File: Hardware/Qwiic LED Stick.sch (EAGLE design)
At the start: 38 parts, among them J2 QWIIC_RA, J4 QWIIC_RA, J6 AVR_SPI_PROG_3X2TESTPOINTS, U2 ATTINY85

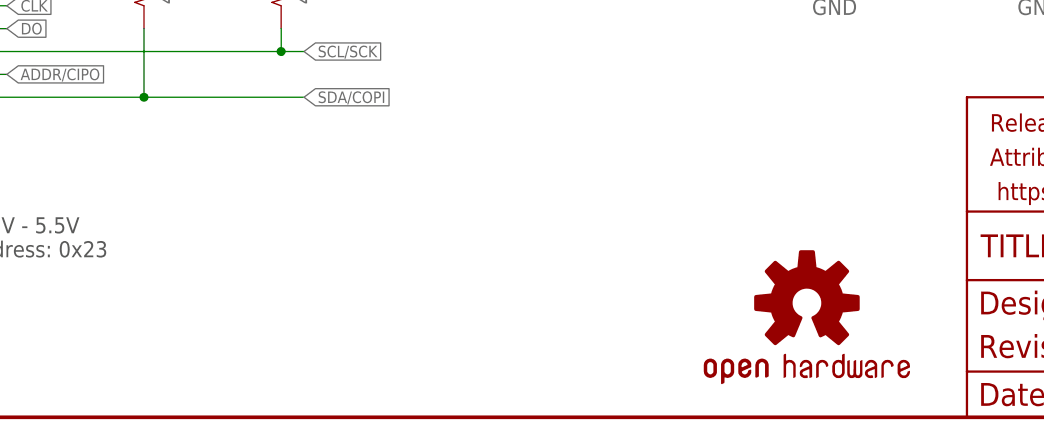
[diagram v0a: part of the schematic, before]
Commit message: Update logos
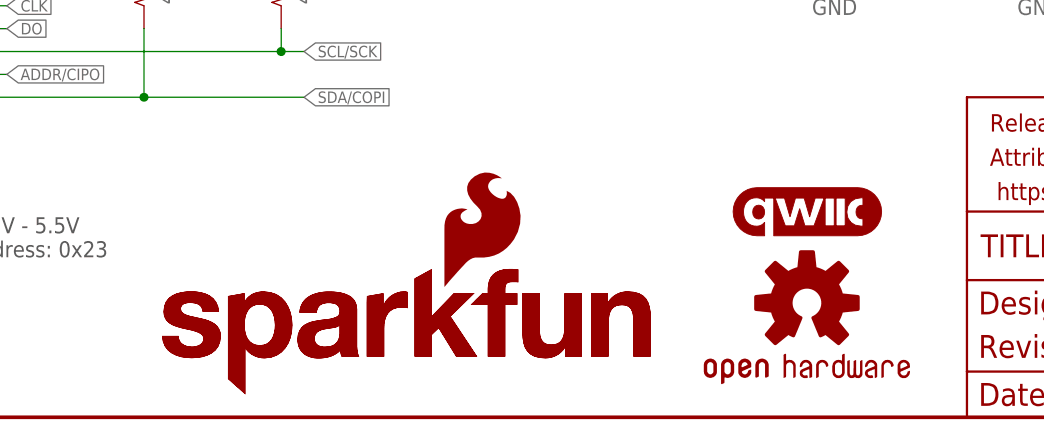
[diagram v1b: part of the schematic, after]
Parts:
- added LOGO2, LOGO5: SFE_LOGO_NAME.2_INCH, SparkFun-Aesthetics:SFE_LOGO_NAME.2_INCH
- added LOGO3: QWIIC_LOGO_5MM, SparkFun-Aesthetics:QWIIC_LOGO_5MM
- added LOGO4: SFE_LOGO_FLAME.2_INCH, SparkFun-Aesthetics:SFE_LOGO_FLAME.2_INCH
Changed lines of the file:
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@@
 <grid distance="0.1" unitdist="inch" unit="inch" style="lines" multiple="1" display="no" altdistance="0.01" altunitdist="inch" altunit="inch"/>
 <layers>
-<layer number="1" name="Top" color="4" fill="1" visible="no" active="no"/>
-<layer number="2" name="Route2" color="1" fill="3" visible="no" active="no"/>
-<layer number="3" name="Route3" color="4" fill="3" visible="no" active="no"/>
-<layer number="4" name="Route4" color="1" fill="4" visible="no" active="no"/>
-<layer number="5" name="Route5" color="4" fill="4" visible="no" active="no"/>
-<layer number="6" name="Route6" color="1" fill="8" visible="no" active="no"/>
-<layer number="7" name="Route7" color="4" fill="8" visible="no" active="no"/>
-<layer number="8" name="Route8" color="1" fill="2" visible="no" active="no"/>
-<layer number="9" name="Route9" color="4" fill="2" visible="no" active="no"/>
-<layer number="10" name="Route10" color="1" fill="7" visible="no" active="no"/>
-<layer number="11" name="Route11" color="4" fill="7" visible="no" active="no"/>
-<layer number="12" name="Route12" color="1" fill="5" visible="no" active="no"/>
-<layer number="13" name="Route13" color="4" fill="5" visible="no" active="no"/>
-<layer number="14" name="Route14" color="1" fill="6" visible="no" active="no"/>
-<layer number="15" name="Route15" color="4" fill="6" visible="no" active="no"/>
-<layer number="16" name="Bottom" color="1" fill="1" visible="no" active="no"/>
-<layer number="17" name="Pads" color="2" fill="1" visible="no" active="no"/>
-<layer number="18" name="Vias" color="2" fill="1" visible="no" active="no"/>
-<layer number="19" name="Unrouted" color="6" fill="1" visible="no" active="no"/>
-<layer number="20" name="Dimension" color="15" fill="1" visible="no" active="no"/>
-<layer number="21" name="tPlace" color="16" fill="1" visible="no" active="no"/>
-<layer number="22" name="bPlace" color="14" fill="1" visible="no" active="no"/>
-<layer number="23" name="tOrigins" color="15" fill="1" visible="no" active="no"/>
-<layer number="24" name="bOrigins" color="15" fill="1" visible="no" active="no"/>
-<layer number="25" name="tNames" color="7" fill="1" visible="no" active="no"/>
-<layer number="26" name="bNames" color="7" fill="1" visible="no" active="no"/>
-<layer number="27" name="tValues" color="7" fill="1" visible="no" active="no"/>
-<layer number="28" name="bValues" color="7" fill="1" visible="no" active="no"/>
+<layer number="1" name="Top" color="4" fill="1" visible="yes" active="no"/>
+<layer number="2" name="Route2" color="1" fill="3" visible="yes" active="no"/>
+<layer number="3" name="Route3" color="4" fill="3" visible="yes" active="no"/>
+<layer number="4" name="Route4" color="1" fill="4" visible="yes" active="no"/>
+<layer number="5" name="Route5" color="4" fill="4" visible="yes" active="no"/>
+<layer number="6" name="Route6" color="1" fill="8" visible="yes" active="no"/>
+<layer number="7" name="Route7" color="4" fill="8" visible="yes" active="no"/>
+<layer number="8" name="Route8" color="1" fill="2" visible="yes" active="no"/>
+<layer number="9" name="Route9" color="4" fill="2" visible="yes" active="no"/>
+<layer number="10" name="Route10" color="1" fill="7" visible="yes" active="no"/>
+<layer number="11" name="Route11" color="4" fill="7" visible="yes" active="no"/>
+<layer number="12" name="Route12" color="1" fill="5" visible="yes" active="no"/>
+<layer number="13" name="Route13" color="4" fill="5" visible="yes" active="no"/>
+<layer number="14" name="Route14" color="1" fill="6" visible="yes" active="no"/>
+<layer number="15" name="Route15" color="4" fill="6" visible="yes" active="no"/>
+<layer number="16" name="Bottom" color="1" fill="1" visible="yes" active="no"/>
+<layer number="17" name="Pads" color="2" fill="1" visible="yes" active="no"/>
+<layer number="18" name="Vias" color="2" fill="1" visible="yes" active="no"/>
+<layer number="19" name="Unrouted" color="6" fill="1" visible="yes" active="no"/>
+<layer number="20" name="Dimension" color="24" fill="1" visible="yes" active="no"/>
+<layer number="21" name="tPlace" color="16" fill="1" visible="yes" active="no"/>
+<layer number="22" name="bPlace" color="14" fill="1" visible="yes" active="no"/>
+<layer number="23" name="tOrigins" color="15" fill="1" visible="yes" active="no"/>
+<layer number="24" name="bOrigins" color="15" fill="1" visible="yes" active="no"/>
+<layer number="25" name="tNames" color="7" fill="1" visible="yes" active="no"/>
+<layer number="26" name="bNames" color="7" fill="1" visible="yes" active="no"/>
+<layer number="27" name="tValues" color="7" fill="1" visible="yes" active="no"/>
+<layer number="28" name="bValues" color="7" fill="1" visible="yes" active="no"/>
 <layer number="29" name="tStop" color="7" fill="3" visible="no" active="no"/>
 <layer number="30" name="bStop" color="7" fill="6" visible="no" active="no"/>
@@
 <layer number="35" name="tGlue" color="7" fill="4" visible="no" active="no"/>
 <layer number="36" name="bGlue" color="7" fill="5" visible="no" active="no"/>
-<layer number="37" name="tTest" color="7" fill="1" visible="no" active="no"/>
-<layer number="38" name="bTest" color="7" fill="1" visible="no" active="no"/>
+<layer number="37" name="tTest" color="7" fill="1" visible="yes" active="no"/>
+<layer number="38" name="bTest" color="7" fill="1" visible="yes" active="no"/>
 <layer number="39" name="tKeepout" color="4" fill="11" visible="no" active="no"/>
 <layer number="40" name="bKeepout" color="1" fill="11" visible="no" active="no"/>
@@
 <layer number="44" name="Drills" color="7" fill="1" visible="no" active="no"/>
 <layer number="45" name="Holes" color="7" fill="1" visible="no" active="no"/>
-<layer number="46" name="Milling" color="3" fill="1" visible="no" active="no"/>
-<layer number="47" name="Measures" color="7" fill="1" visible="no" active="no"/>
-<layer number="48" name="Document" color="7" fill="1" visible="no" active="no"/>
-<layer number="49" name="Reference" color="7" fill="1" visible="no" active="no"/>
-<layer number="50" name="dxf" color="7" fill="1" visible="no" active="no"/>
-<layer number="51" name="tDocu" color="6" fill="1" visible="no" active="no"/>
-<layer number="52" name="bDocu" color="7" fill="1" visible="no" active="no"/>
-<layer number="53" name="tGND_GNDA" color="7" fill="9" visible="no" active="no"/>
-<layer number="54" name="bGND_GNDA" color="1" fill="9" visible="no" active="no"/>
-<layer number="56" name="wert" color="7" fill="1" visible="no" active="no"/>
-<layer number="57" name="tCAD" color="7" fill="1" visible="no" active="no"/>
-<layer number="58" name="bCopper" color="7" fill="1" visible="no" active="no"/>
-<layer number="59" name="tCarbon" color="7" fill="1" visible="no" active="no"/>
-<layer number="60" name="bCarbon" color="7" fill="1" visible="no" active="no"/>
+<layer number="46" name="Milling" color="3" fill="1" visible="yes" active="no"/>
+<layer number="47" name="Measures" color="7" fill="1" visible="yes" active="no"/>
+<layer number="48" name="Document" color="7" fill="1" visible="yes" active="no"/>
+<layer number="49" name="Reference" color="7" fill="1" visible="yes" active="no"/>
+<layer number="50" name="dxf" color="7" fill="1" visible="yes" active="no"/>
+<layer number="51" name="tDocu" color="6" fill="1" visible="yes" active="no"/>
+<layer number="52" name="bDocu" color="7" fill="1" visible="yes" active="no"/>
+<layer number="53" name="tGND_GNDA" color="7" fill="9" visible="yes" active="no"/>
+<layer number="54" name="bGND_GNDA" color="1" fill="9" visible="yes" active="no"/>
+<layer number="56" name="wert" color="7" fill="1" visible="yes" active="no"/>
+<layer number="57" name="tCAD" color="7" fill="1" visible="yes" active="no"/>
+<layer number="58" name="bCopper" color="7" fill="1" visible="yes" active="no"/>
+<layer number="59" name="tCarbon" color="7" fill="1" visible="yes" active="no"/>
+<layer number="60" name="bCarbon" color="7" fill="1" visible="yes" active="no"/>
 <layer number="88" name="SimResults" color="9" fill="1" visible="yes" active="yes"/>
 <layer number="89" name="SimProbes" color="9" fill="1" visible="yes" active="yes"/>
@@
 <part name="GND12" library="SparkFun-PowerSymbols" deviceset="GND" device=""/>
 <part name="SUPPLY1" library="SparkFun-PowerSymbols" deviceset="3.3V" device=""/>
+<part name="LOGO2" library="SparkFun-Aesthetics" deviceset="SFE_LOGO_NAME" device=".2_INCH"/>
+<part name="LOGO3" library="SparkFun-Aesthetics" deviceset="QWIIC_LOGO" device="_5MM" value="QWIIC_LOGO_5MM"/>
+<part name="LOGO4" library="SparkFun-Aesthetics" deviceset="SFE_LOGO_FLAME" device=".2_INCH"/>
+<part name="LOGO5" library="SparkFun-Aesthetics" deviceset="SFE_LOGO_NAME" device=".2_INCH"/>
 </parts>
 <sheets>
@@
 <attribute name="VALUE" x="177.8" y="139.954" size="1.778" layer="96" align="bottom-center"/>
 </instance>
+<instance part="LOGO2" gate="G$1" x="55.88" y="2.54" smashed="yes"/>
+<instance part="LOGO3" gate="G$1" x="129.54" y="22.86" smashed="yes"/>
+<instance part="LOGO4" gate="G$1" x="88.9" y="13.97" smashed="yes"/>
+<instance part="LOGO5" gate="G$1" x="55.88" y="2.54" smashed="yes"/>
 </instances>
 <busses>

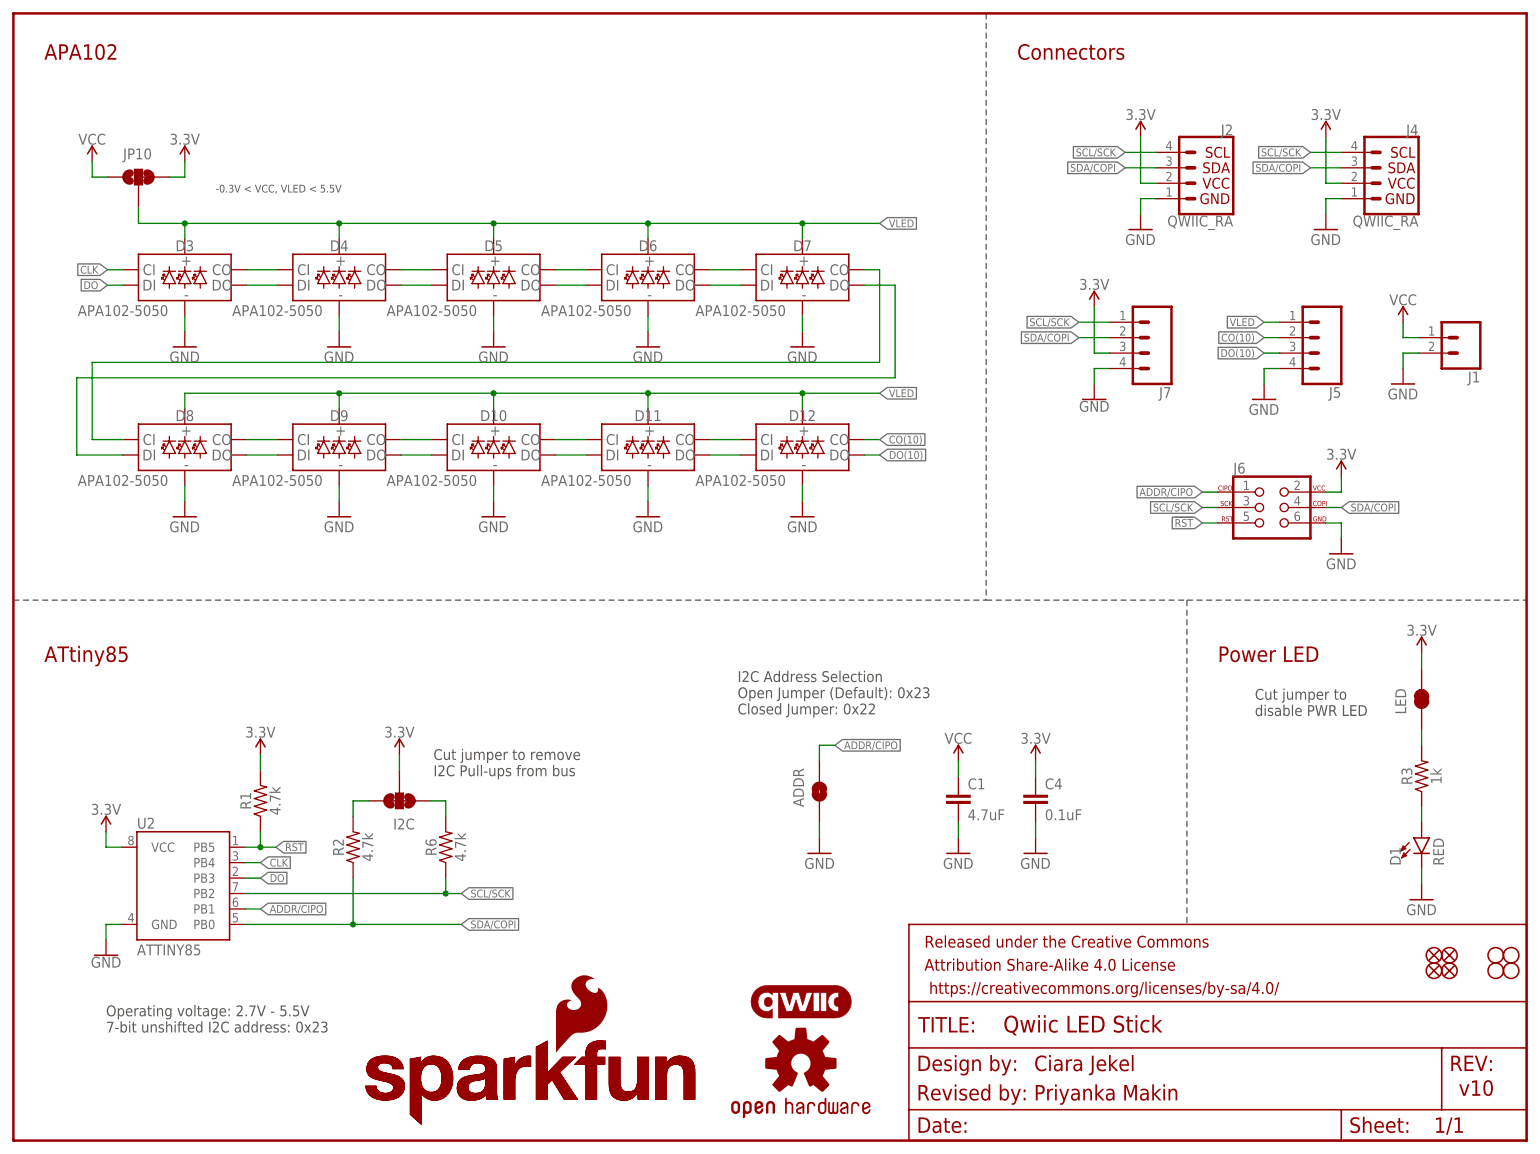
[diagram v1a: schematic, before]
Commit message: Design review changes:
Sch:
Re-number diodes starting at 0
Change VCC net label to VIN
Added 4 more stand off holes for 1x1 qwiic

Board:
Added measures for PTH and LEDs
Thickened up the VIN trace to 0.02
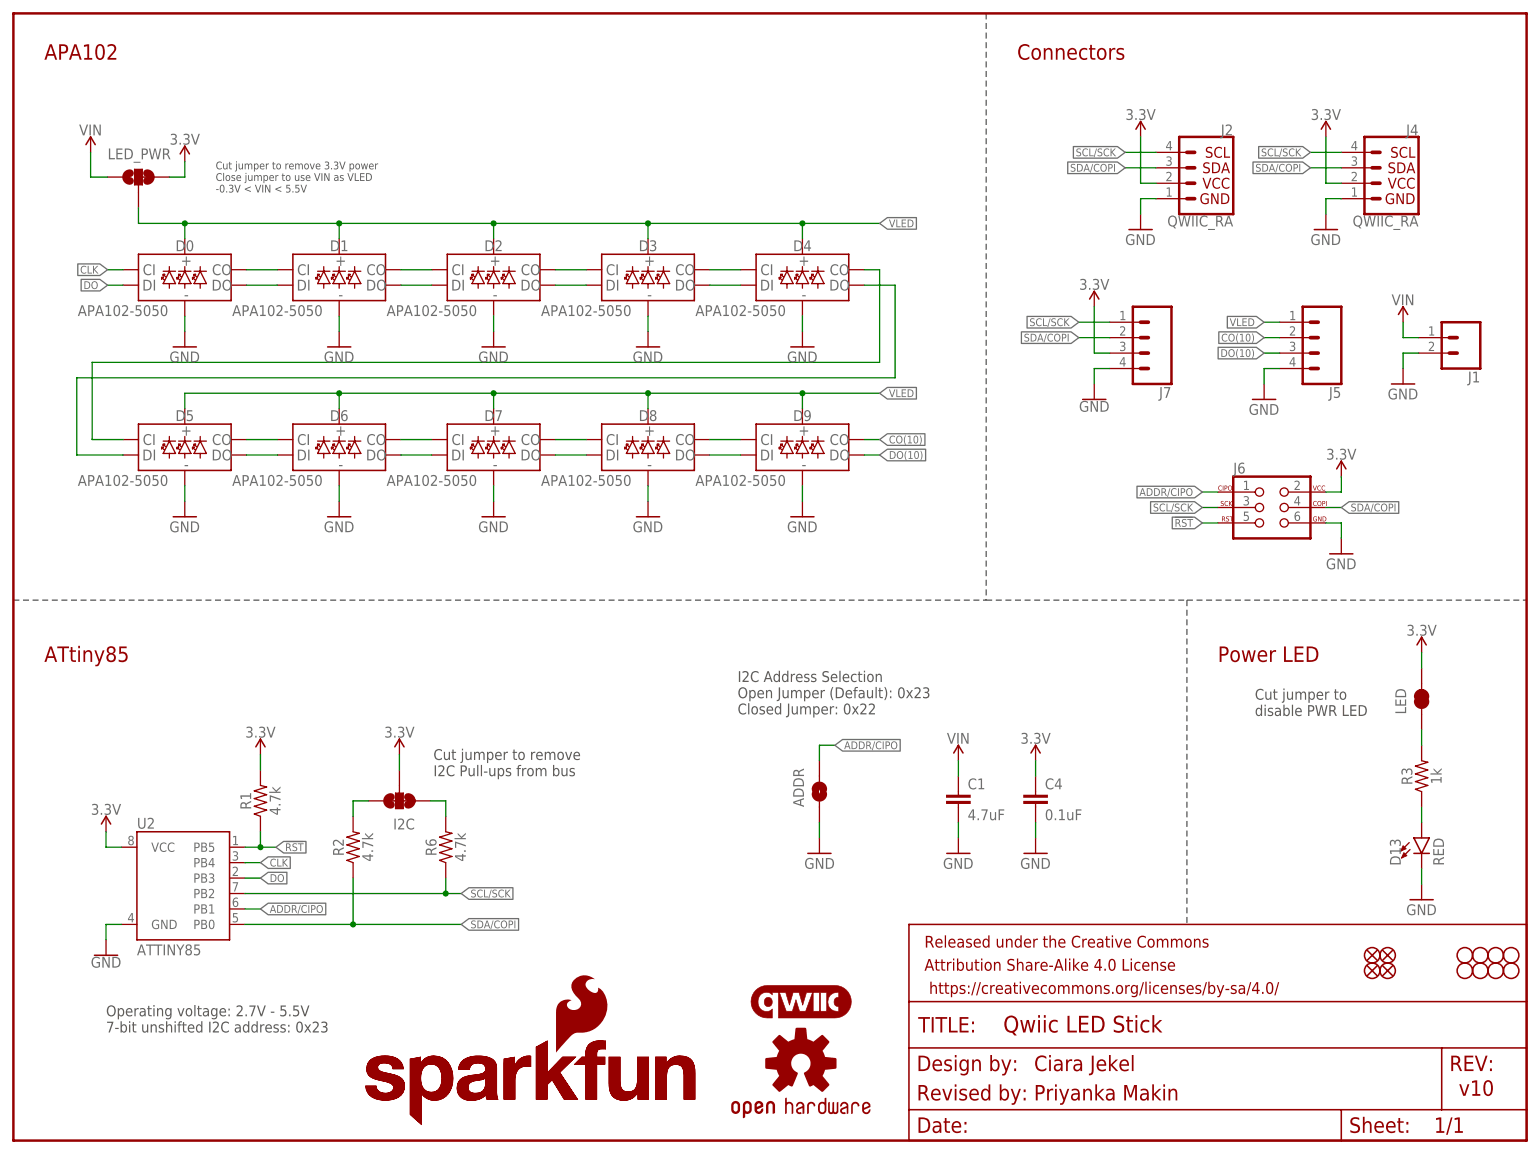
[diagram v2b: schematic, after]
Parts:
- removed D10, D11, D12: APA102-5050, SparkFun-LED:APA102-5050
- added D0, D2: APA102-5050, SparkFun-LED:APA102-5050
- added D13: RED, SparkFun-LED:LED-RED0603
- added H1, H2, H3, H4: STAND-OFF, SparkFun-Hardware:STAND-OFF
- D1: value RED -> APA102-5050; device SparkFun-LED:LED-RED0603 -> SparkFun-LED:APA102-5050
- renumbered JP10 to LED_PWR
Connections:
- net VCC renamed VIN
- removed net N$10 (its old number): D10.CO, D11.CI
- removed net N$11 (its old number): D10.DO, D11.DI
- removed net N$12 (its old number): D10.CI, D9.CO
- removed net N$13 (its old number): D10.DI, D9.DO
- removed net N$8 (its old number): D11.DO, D12.DI
- removed net N$9 (its old number): D11.CO, D12.CI
- new net N$20: D2.DO, D3.DI
- new net N$21: D2.CO, D3.CI
- new net N$22: D1.DO, D2.DI
- new net N$23: D1.CO, D2.CI
- new net N$24: D0.CO, D1.CI
- new net N$25: D0.DO, D1.DI
- net CLK: now also D0.CI; no longer D3.CI
- net CO(10): now also D9.CO; no longer D12.CO
- net DO: now also D0.DI; no longer D3.DI
- net DO(10): now also D9.DO; no longer D12.DO
- net GND: now also D0.GND, D1.GND, D13.C, D2.GND; no longer D1.C, D10.GND, D11.GND, D12.GND
- net N$3: now also D13.A; no longer D1.A
- net VLED: now also D0.VCC, D1.VCC, D2.VCC; no longer D10.VCC, D11.VCC, D12.VCC
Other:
- note added: "Cut jumper to remove 3.3V power Close jumper to use VIN as VLED -0.3V < VIN < 5.5V"
- note removed: "-0.3V < VCC, VLED < 5.5V"
- moved on the sheet: D3, D4, D5, D6, D7, D8, D9

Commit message: Checklist
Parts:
- renumbered D13 to D10
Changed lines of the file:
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@@
 <part name="R3" library="SparkFun-Resistors" deviceset="1KOHM" device="-0603-1/10W-1%" value="1k"/>
 <part name="SUPPLY10" library="SparkFun-PowerSymbols" deviceset="3.3V" device=""/>
-<part name="D13" library="SparkFun-LED" deviceset="LED-RED" device="0603" value="RED"/>
+<part name="D10" library="SparkFun-LED" deviceset="LED-RED" device="0603" value="RED"/>
 <part name="GND3" library="SparkFun-PowerSymbols" deviceset="GND" device=""/>
 <part name="D0" library="SparkFun-LED" deviceset="APA102" device="-5050"/>
@@
 <attribute name="VALUE" x="231.648" y="83.058" size="1.778" layer="96" font="vector" align="bottom-center"/>
 </instance>
-<instance part="D13" gate="G$1" x="231.648" y="49.784" smashed="yes">
+<instance part="D10" gate="G$1" x="231.648" y="49.784" smashed="yes">
 <attribute name="NAME" x="228.219" y="45.212" size="1.778" layer="95" font="vector" rot="R90"/>
 <attribute name="VALUE" x="233.553" y="45.212" size="1.778" layer="96" font="vector" rot="R90" align="top-left"/>
@@
 </segment>
 <segment>
-<pinref part="D13" gate="G$1" pin="C"/>
+<pinref part="D10" gate="G$1" pin="C"/>
 <pinref part="GND3" gate="1" pin="GND"/>
 <wire x1="231.648" y1="42.164" x2="231.648" y2="44.704" width="0.1524" layer="91"/>
@@
 <segment>
 <pinref part="R3" gate="G$1" pin="1"/>
-<pinref part="D13" gate="G$1" pin="A"/>
+<pinref part="D10" gate="G$1" pin="A"/>
 <wire x1="231.648" y1="52.324" x2="231.648" y2="54.864" width="0.1524" layer="91"/>
 </segment>

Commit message: Update Qwiic LED Stick.sch
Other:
- note added: "Cut jumper to remove 3.3V power Close jumper to use VIN as VLED VIN Max: 5.5V"
- note removed: "Cut jumper to remove 3.3V power Close jumper to use VIN as VLED -0.3V < VIN < 5.5V"
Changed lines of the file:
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@@
 <text x="33.274" y="155.956" size="1.27" layer="97" font="vector">Cut jumper to remove 3.3V power
 Close jumper to use VIN as VLED
--0.3V &lt; VIN &lt; 5.5V</text>
+VIN Max: 5.5V</text>
 <text x="148.59" y="6.604" size="2.54" layer="94" font="vector">Revised by: Priyanka Makin</text>
 <wire x1="160.02" y1="88.9" x2="193.04" y2="88.9" width="0.2032" layer="97" style="longdash"/>
